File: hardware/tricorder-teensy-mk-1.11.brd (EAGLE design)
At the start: 50.8 x 22.9 mm, 24 parts, among them U1 MCP73831, U2 LTC2941

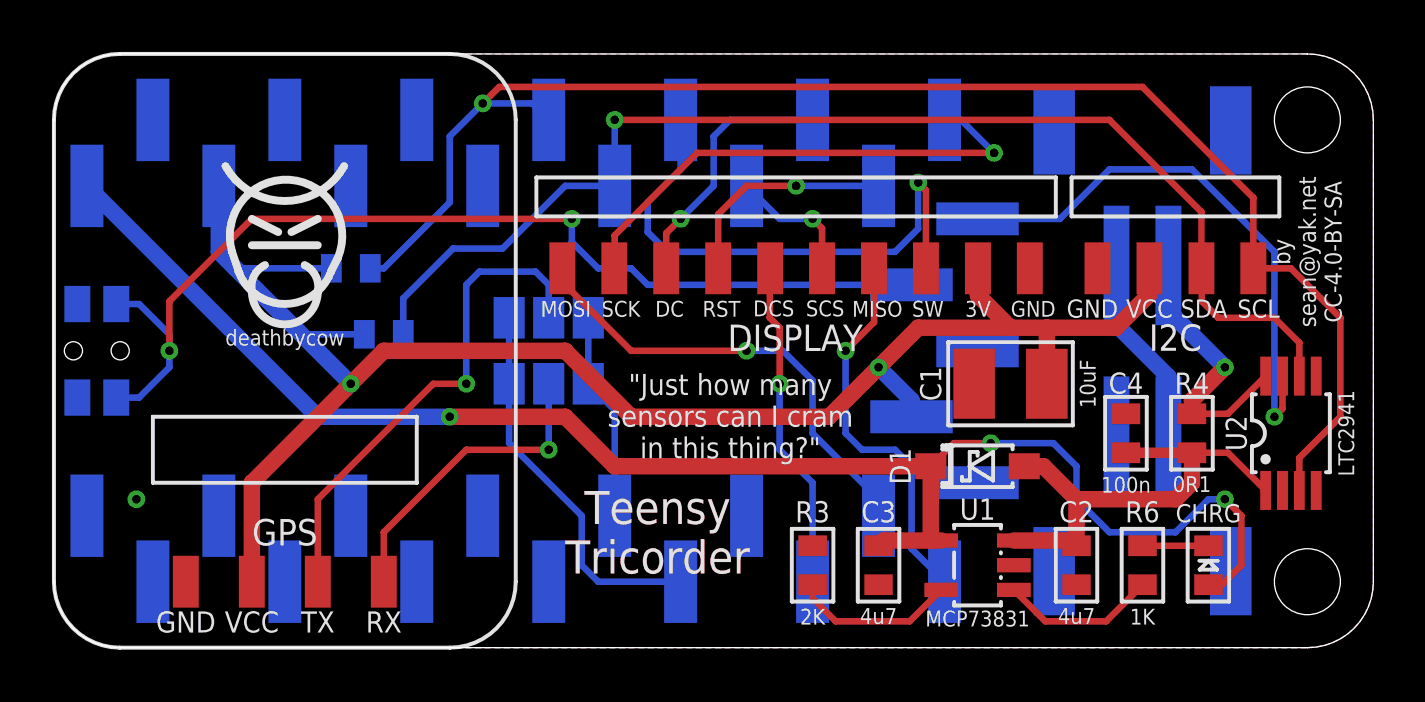
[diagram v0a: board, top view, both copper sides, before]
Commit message: new revision with LTC2942 instead of '41
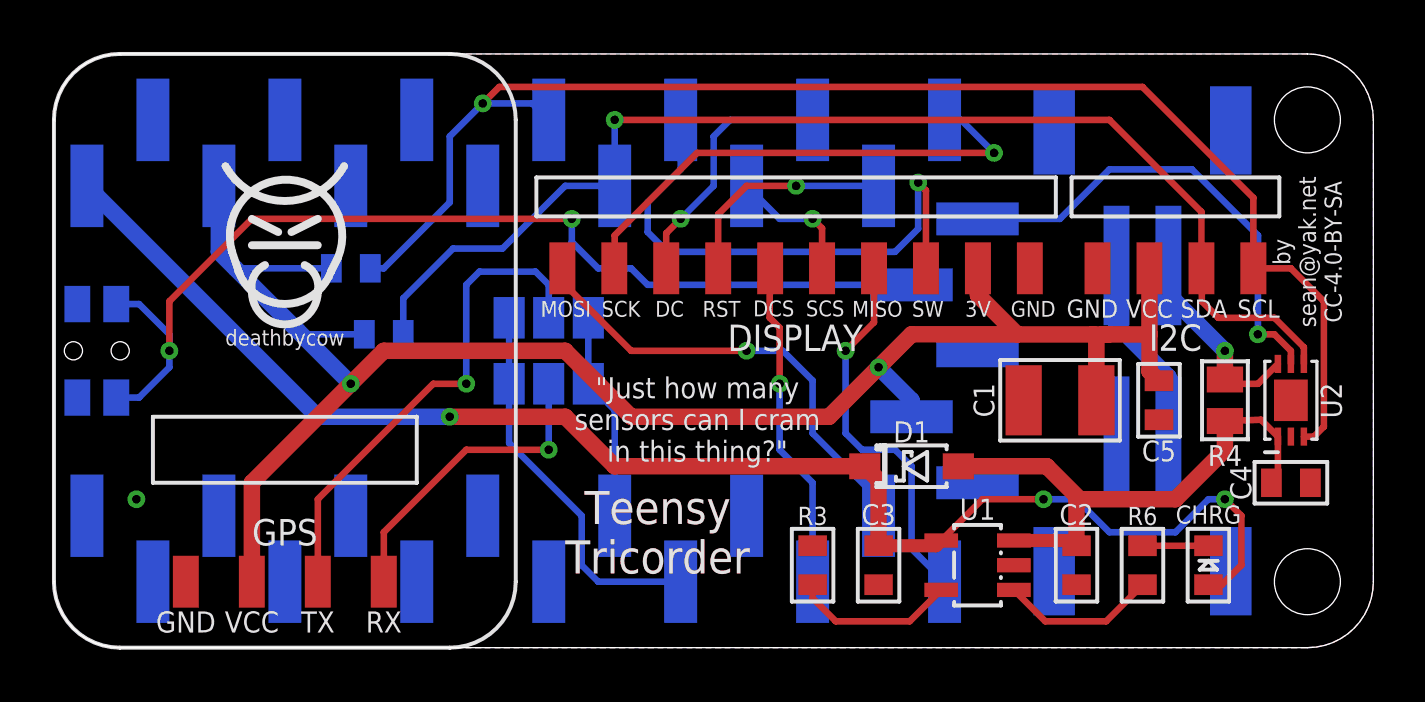
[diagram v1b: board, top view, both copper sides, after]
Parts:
- added C5: 100n, a_parts:C0603-TIGHTER
- C1: value 10uF -> 100uF
- GPS_RX_ALT, GPS_TX_ALT: value (none) -> JUMPER-PAD-3-NOFULL_BOX_SILK
- R4: device a_parts:R0603-TIGHTER -> a_parts:R0805-TIGHTER
- TEENSY: value TEENSY-3.1-OUTERSMT -> TEENSY-3.1-OUTERSMD
- U2: device a_parts:MSOP-8 -> a_parts:DFN200X300X50-7N
- moved C4 6.63 mm to (47.6, 6.35), turned to 0 degrees
- moved D1 2.54 mm to (33.0, 6.99)
- moved C1 2.01 mm to (38.7, 9.53), turned to 0 degrees
- moved R4 1.80 mm to (45.1, 9.53)
- moved U2 1.27 mm to (47.6, 9.53), turned to 0 degrees
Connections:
- net N$1 renamed STAT
- net N$2 renamed CHARGING
- net N$3 renamed BEFORE_SW
- net N$4 renamed CURRENT_SET
- removed net N$5: PWR_SW.1, R4.1, U2.8
- new net AFTER_SW: PWR_SW.1, R4.1, U2.6
- net !AL/CC: now also U2.5; no longer U2.7
- net 3.3V: now also C1.2, C5.1; no longer C1.1
- net GND: now also C1.1, C5.2; no longer C1.2
- net SDA: now also U2.4; no longer U2.6
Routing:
- net N$5: track 10.6 -> 0.00 mm, vias 1 -> 0
- net AFTER_SW: track 0.00 -> 7.73 mm, vias 0 -> 1
- net 3.3V: track 67.9 -> 71.8 mm
- net VUSB: track 61.1 -> 57.2 mm
- net !AL/CC: track 21.6 -> 18.5 mm
- net VBAT: track 18.7 -> 21.3 mm
- net SCL: track 57.1 -> 54.7 mm
